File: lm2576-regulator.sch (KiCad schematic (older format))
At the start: 9 parts, among them J1 Barrel Jack, J2 KLS2, U1 LM2576HVS-5

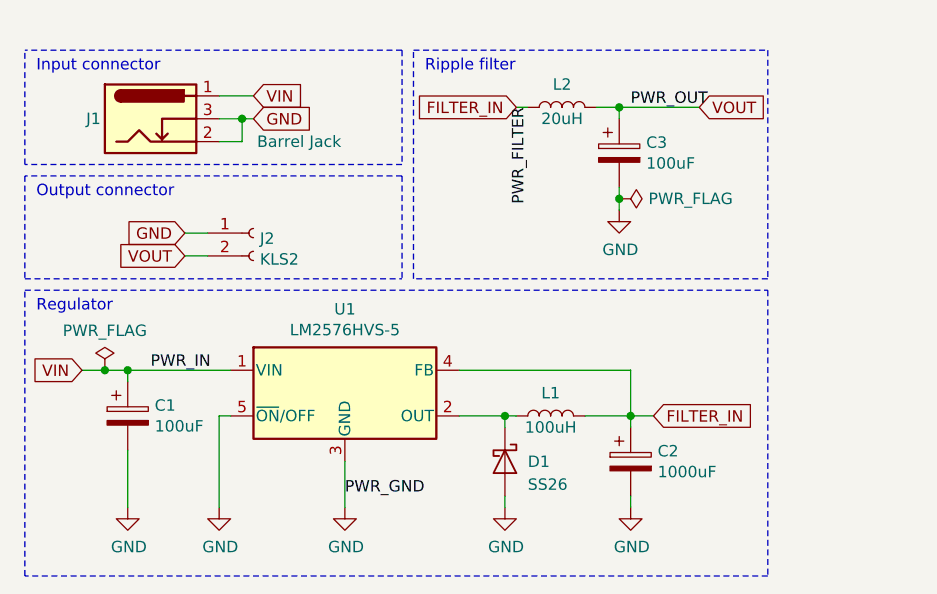
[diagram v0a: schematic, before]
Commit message: Made improvements for production on a factory
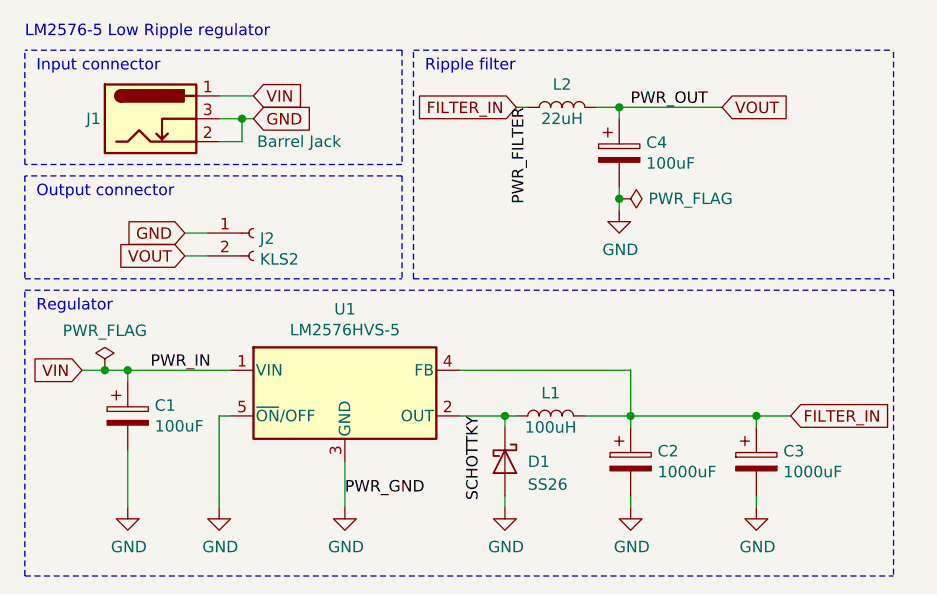
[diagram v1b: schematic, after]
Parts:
- added C3: 1000uF, Capacitor_SMD:CP_Elec_10x10.5, symbol Device:CP
- L2: value 20uH -> 22uH
- renumbered C3 to C4
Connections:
- net FILTER_IN: now also C3.1
- net GND: now also C3.2
- net SCHOTTKY: now reaches D1.1 (K), L1.1, U1.2 (OUT)
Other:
- note added: "LM2576-5 Low Ripple regulator"
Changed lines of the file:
@@
 Connection ~ 6400 4200
 $Comp
-L Device:CP C3
+L Device:CP C4
 U 1 1 5E362070
 P 6350 3050
-F 0 "C3" H 6468 3096 50  0000 L CNN
+F 0 "C4" H 6468 3096 50  0000 L CNN
 F 1 "100uF" H 6468 3005 50  0000 L CNN
 F 2 "Capacitor_SMD:CP_Elec_8x10" H 6388 2900 50  0001 C CNN
@@
 P 6100 2850
 F 0 "L2" V 6200 2850 50  0000 C CNN
-F 1 "20uH" V 6050 2850 50  0000 C CNN
+F 1 "22uH" V 6050 2850 50  0000 C CNN
 F 2 "Inductor_SMD:L_12x12mm_H8mm" H 6100 2850 50  0001 C CNN
 F 3 "~" H 6100 2850 50  0001 C CNN
@@
 	4200 4000 4100 4000
 Connection ~ 4200 4000
-Text GLabel 6700 2850 2    50   Input ~ 0
+Text GLabel 6800 2850 2    50   Input ~ 0
 VOUT
 Wire Wire Line
-	6500 4200 6400 4200
+	7100 4200 6950 4200
 Wire Wire Line
 	6400 4550 6400 4600
@@
 	1    0    0    -1
 $EndComp
-Text GLabel 6500 4200 2    50   Input ~ 0
+Text GLabel 7100 4200 2    50   Input ~ 0
 FILTER_IN
 Text GLabel 5900 2850 0    50   Input ~ 0
 FILTER_IN
 Wire Wire Line
-	6350 2850 6700 2850
+	6350 2850 6800 2850
 Connection ~ 6350 2850
 Wire Wire Line
@@
 Wire Wire Line
 	4450 3500 4550 3500
-Wire Notes Line
-	3750 3650 7000 3650
-Wire Notes Line
-	7000 3650 7000 4900
-Wire Notes Line
-	7000 4900 3750 4900
 Wire Notes Line
 	3750 4900 3750 3650
 Text Notes 3800 3750 0    50   ~ 0
 Regulator
-Wire Notes Line
-	5450 2600 7000 2600
-Wire Notes Line
-	7000 2600 7000 3600
-Wire Notes Line
-	7000 3600 5450 3600
 Wire Notes Line
 	5450 3600 5450 2600
@@
 Wire Wire Line
 	4750 2800 4600 2800
+$Comp
+L Device:CP C3
+U 1 1 5E3B4737
+P 6950 4400
+F 0 "C3" H 7068 4446 50  0000 L CNN
+F 1 "1000uF" H 7068 4355 50  0000 L CNN
+F 2 "Capacitor_SMD:CP_Elec_10x10.5" H 6988 4250 50  0001 C CNN
+F 3 "~" H 6950 4400 50  0001 C CNN
+	1    6950 4400
+	1    0    0    -1
+$EndComp
+Wire Wire Line
+	6950 4250 6950 4200
+Connection ~ 6950 4200
+Wire Wire Line
+	6950 4200 6400 4200
+$Comp
+L power:GND #PWR0107
+U 1 1 5E3B547D
+P 6950 4600
+F 0 "#PWR0107" H 6950 4350 50  0001 C CNN
+F 1 "GND" H 6955 4427 50  0000 C CNN
+F 2 "" H 6950 4600 50  0001 C CNN
+F 3 "" H 6950 4600 50  0001 C CNN
+	1    6950 4600
+	1    0    0    -1
+$EndComp
+Wire Wire Line
+	6950 4550 6950 4600
+Wire Notes Line
+	7550 3650 7550 4900
+Wire Notes Line
+	3750 3650 7550 3650
+Wire Notes Line
+	3750 4900 7550 4900
+Wire Notes Line
+	7550 3600 7550 2600
+Wire Notes Line
+	5450 3600 7550 3600
+Wire Notes Line
+	5450 2600 7550 2600
+Text Label 5750 4200 3    50   ~ 0
+SCHOTTKY
+Text Notes 3750 2550 0    50   ~ 0
+LM2576-5 Low Ripple regulator
 $EndSCHEMATC

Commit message: Modified after review of Alexander
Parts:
- D1: footprint Diode_SMD:D_SMB -> Diode_SMD:D_SMC
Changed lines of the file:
@@
 F 0 "D1" V 5850 4500 50  0000 L CNN
 F 1 "SS26" V 5950 4500 50  0000 L CNN
-F 2 "Diode_SMD:D_SMB" H 5850 4225 50  0001 C CNN
+F 2 "Diode_SMD:D_SMC" H 5850 4225 50  0001 C CNN
 F 3 "http://www.vishay.com/docs/88526/1n5820.pdf" H 5850 4400 50  0001 C CNN
 	1    5850 4400
